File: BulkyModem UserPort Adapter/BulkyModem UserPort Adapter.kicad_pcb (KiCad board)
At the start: 2 copper layers, 70.7 x 35 mm, 7 parts, among them J1 C64_UserPort, J2 Temporary, J3 C64_Modem_IDC, M1 Mounting, M2 Mounting, M3 Mounting, M4 Mounting

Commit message: Add DCD
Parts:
- moved J3 10.5 mm to (156.6, 78.1), turned to 270 degrees
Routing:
- net Net-(J2-Pad4): track 7.40 -> 28.4 mm
- net Net-(J2-Pad6): track 7.40 -> 25.9 mm
- net Net-(J2-Pad8): track 7.40 -> 23.4 mm
- net Net-(J2-Pad10): track 7.40 -> 18.9 mm
- net RX: track 51.7 -> 43.7 mm
- net RTS: track 24.1 -> 26.7 mm, vias 0 -> 1
- net TX: track 48.8 -> 46.3 mm
- net DCD: track 20.3 -> 22.3 mm
- net Net-(J1-Pad6): track 25.7 -> 24.5 mm
- net CTS: track 20.8 -> 21.9 mm
- net Net-(J1-Pad2): track 42.9 -> 43.2 mm, vias 2 -> 1

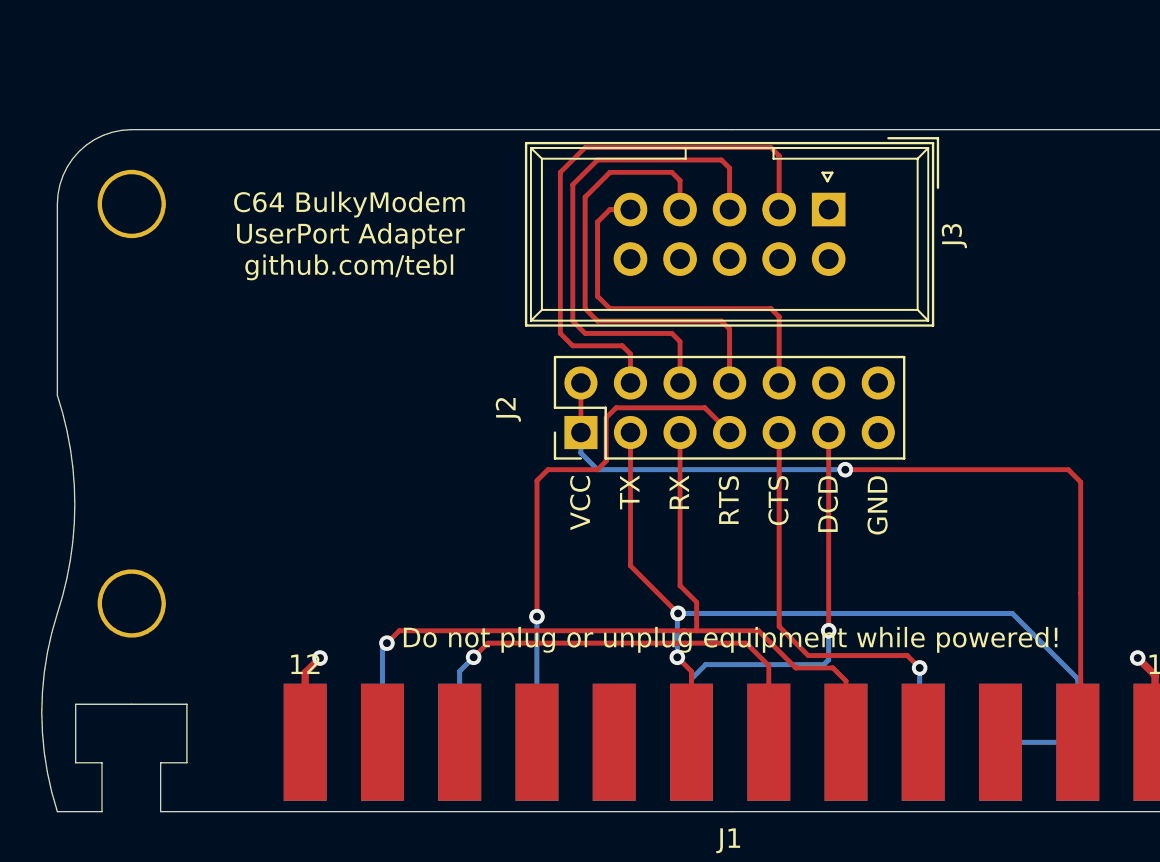
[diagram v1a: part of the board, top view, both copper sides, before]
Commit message: Changed IDC pin count
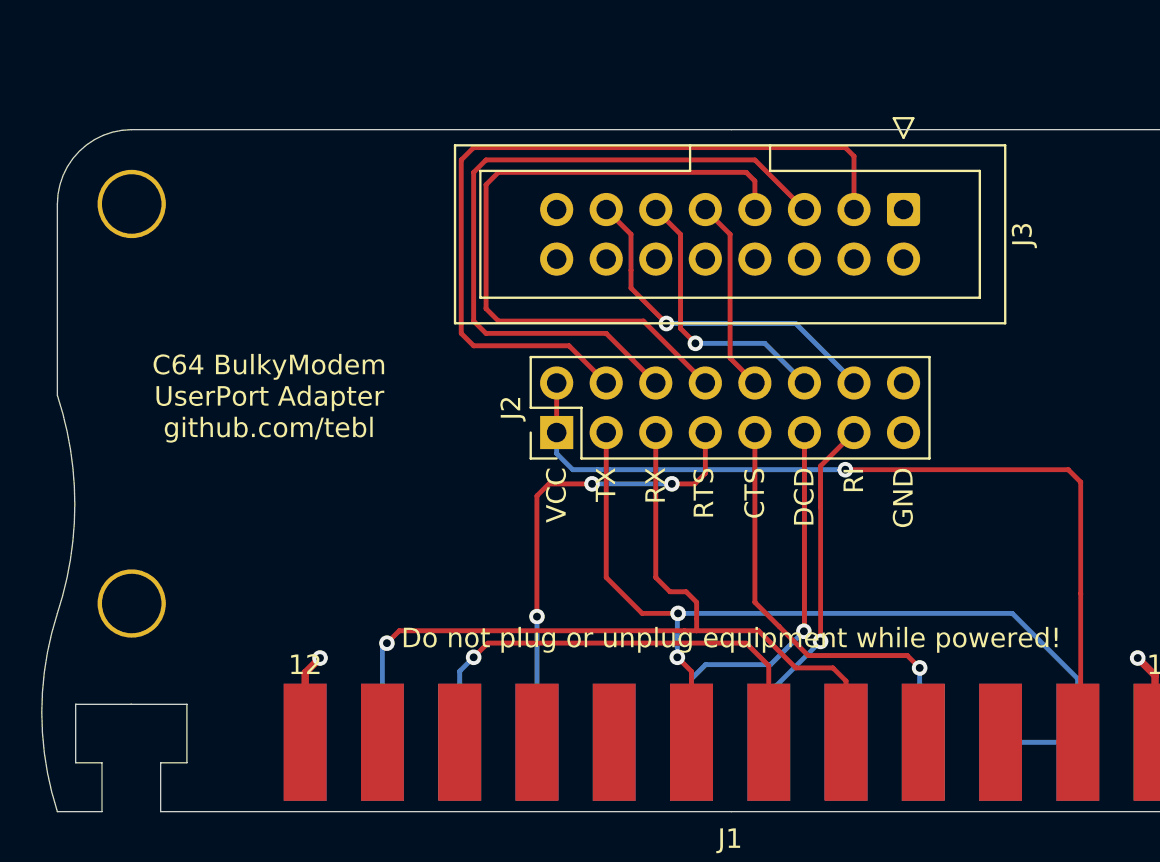
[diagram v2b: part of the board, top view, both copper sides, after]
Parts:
- J2: footprint Connector_PinHeader_2.54mm:PinHeader_2x07_P2.54mm_Vertical -> Connector_PinHeader_2.54mm:PinHeader_2x08_P2.54mm_Vertical
- J3: footprint BulkyModem:C64_Adapter_IDC -> BulkyModem:UserPort_Adapter_IDC
- moved J3 3.84 mm to (160.5, 78.1)
- moved J2 1.24 mm to (142.7, 89.5)
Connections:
- J1 pad 10: (no net) -> Net-(J1-Pad10)
- J1 pad 11: (no net) -> Net-(J1-Pad11)
- J1 pad 3: (no net) -> Net-(J1-Pad3)
- J1 pad 4: (no net) -> Net-(J1-Pad4)
- J1 pad 8: (no net) -> Net-(J1-Pad8)
- J1 pad 9: (no net) -> Net-(J1-Pad9)
- J1 pad E: (no net) -> Net-(J1-PadE)
- J1 pad F: (no net) -> RI
- J1 pad J: (no net) -> Net-(J1-PadJ)
- J2 pad 12: (no net) -> Net-(J2-Pad12)
- J2 pad 13: GND -> RI
- J2 pad 14: GND -> Net-(J2-Pad14)
- J3 pad 1: (no net) -> Net-(J3-Pad1)
- J3 pad 6: GND -> Net-(J2-Pad12)
- J3 pad 7: GND -> Net-(J2-Pad14)
- J3 pad 8: GND -> Net-(J3-Pad8)
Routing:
- net Net-(J2-Pad14): track 0.00 -> 18.0 mm, vias 0 -> 1
- net RI: track 0.00 -> 17.7 mm, vias 0 -> 1
- net Net-(J2-Pad12): track 0.00 -> 14.1 mm, vias 0 -> 1
- net Net-(J2-Pad4): track 28.4 -> 40.7 mm
- net Net-(J2-Pad8): track 23.4 -> 34.9 mm
- net Net-(J2-Pad6): track 25.9 -> 36.5 mm
- net Net-(J2-Pad10): track 18.9 -> 9.94 mm
- net RTS: track 26.7 -> 23.8 mm, vias 1 -> 3
- net DCD: track 22.3 -> 20.2 mm
- net TX: track 46.3 -> 47.9 mm
- net Net-(J1-Pad2): track 43.2 -> 44.5 mm
- net RX: track 43.7 -> 44.7 mm
- net CTS: track 21.9 -> 22.4 mm
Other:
- board text added: "RI"

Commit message: Alternate panel designs
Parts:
- removed J2: Temporary, Connector_PinHeader_2.54mm:PinHeader_2x08_P2.54mm_Vertical
- added G***: LOGO, artwork:BulkyModem_small, B.Cu at (151.6, 90.7)
- added JP1: UP9600, solder_bridge:bridge, F.Cu at (157.5, 97.5)
- added JP2: UP9600, solder_bridge:bridge, F.Cu at (149.6, 97.5)
- moved J3 5.00 mm to (160.5, 83.1)
- moved M3 5.00 mm to (182.4, 82.8)
- moved M4 5.00 mm to (120.9, 82.8)
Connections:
- J1 pad 10: Net-(J1-Pad10) -> (no net)
- J1 pad 11: Net-(J1-Pad11) -> (no net)
- J1 pad 2: Net-(J1-Pad2) -> (no net)
- J1 pad 3: Net-(J1-Pad3) -> (no net)
- J1 pad 4: Net-(J1-Pad4) -> (no net)
- J1 pad 5: RX -> Net-(J1-Pad5)
- J1 pad 7: TX -> Net-(J1-Pad7)
- J1 pad 8: Net-(J1-Pad8) -> (no net)
- J1 pad 9: Net-(J1-Pad9) -> (no net)
- J1 pad B: TX -> TXD
- J1 pad C: TX -> TXD
- J1 pad E: Net-(J1-PadE) -> (no net)
- J1 pad J: Net-(J1-PadJ) -> (no net)
- J1 pad M: RX -> RXD
- J3 pad 1: Net-(J3-Pad1) -> (no net)
- J3 pad 16: Net-(J3-Pad16) -> (no net)
- J3 pad 2: Net-(J2-Pad4) -> TXD
- J3 pad 3: Net-(J2-Pad6) -> RXD
- J3 pad 4: Net-(J2-Pad8) -> RTS
- J3 pad 5: Net-(J2-Pad10) -> CTS
- J3 pad 6: Net-(J2-Pad12) -> DCD
- J3 pad 7: Net-(J2-Pad14) -> RI
- J3 pad 8: Net-(J3-Pad8) -> (no net)
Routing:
- net RXD: track 0.00 -> 74.0 mm, vias 0 -> 2
- net TXD: track 0.00 -> 59.8 mm, vias 0 -> 1
- net TX: track 47.9 -> 0.00 mm, vias 2 -> 0
- net RX: track 44.7 -> 0.00 mm, vias 1 -> 0
- net Net-(J1-Pad2): track 44.5 -> 0.00 mm, vias 1 -> 0
- net Net-(J2-Pad4): track 40.7 -> 0.00 mm
- net Net-(J2-Pad6): track 36.5 -> 0.00 mm
- net Net-(J2-Pad8): track 34.9 -> 0.00 mm
- net Net-(J2-Pad14): track 18.0 -> 0.00 mm, vias 1 -> 0
- net Net-(J2-Pad12): track 14.1 -> 0.00 mm, vias 1 -> 0
- net RI: track 17.7 -> 30.9 mm
- net RTS: track 23.8 -> 36.9 mm, vias 3 -> 1
- net CTS: track 22.4 -> 34.2 mm
- net Net-(J2-Pad10): track 9.94 -> 0.00 mm
- net Net-(J1-Pad5): track 0.00 -> 7.89 mm
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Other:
- board size 70.7 x 35 mm -> 70.7 x 30 mm
- rule trace_min: 0.2 -> 0
- board text added: "Designed for use with"
- board text added: "Link for UP9600"
- board text removed: "CTS"
- board text removed: "DCD"
- board text removed: "Designed for use with BulkyModem."
- board text removed: "GND"
- board text removed: "RI"
- board text removed: "RTS"
- board text removed: "RX"
- board text removed: "TX"
- board text removed: "VCC"

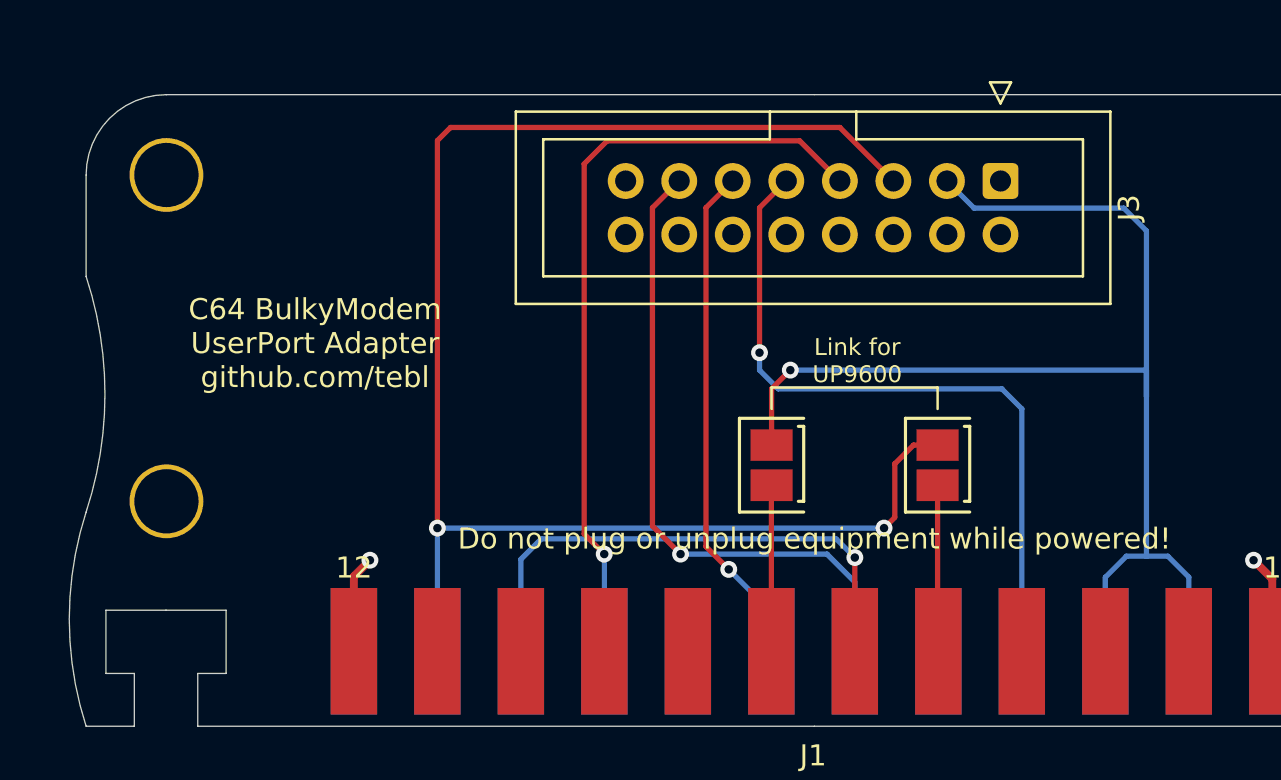
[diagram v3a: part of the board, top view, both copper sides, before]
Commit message: Updated UserPort layout
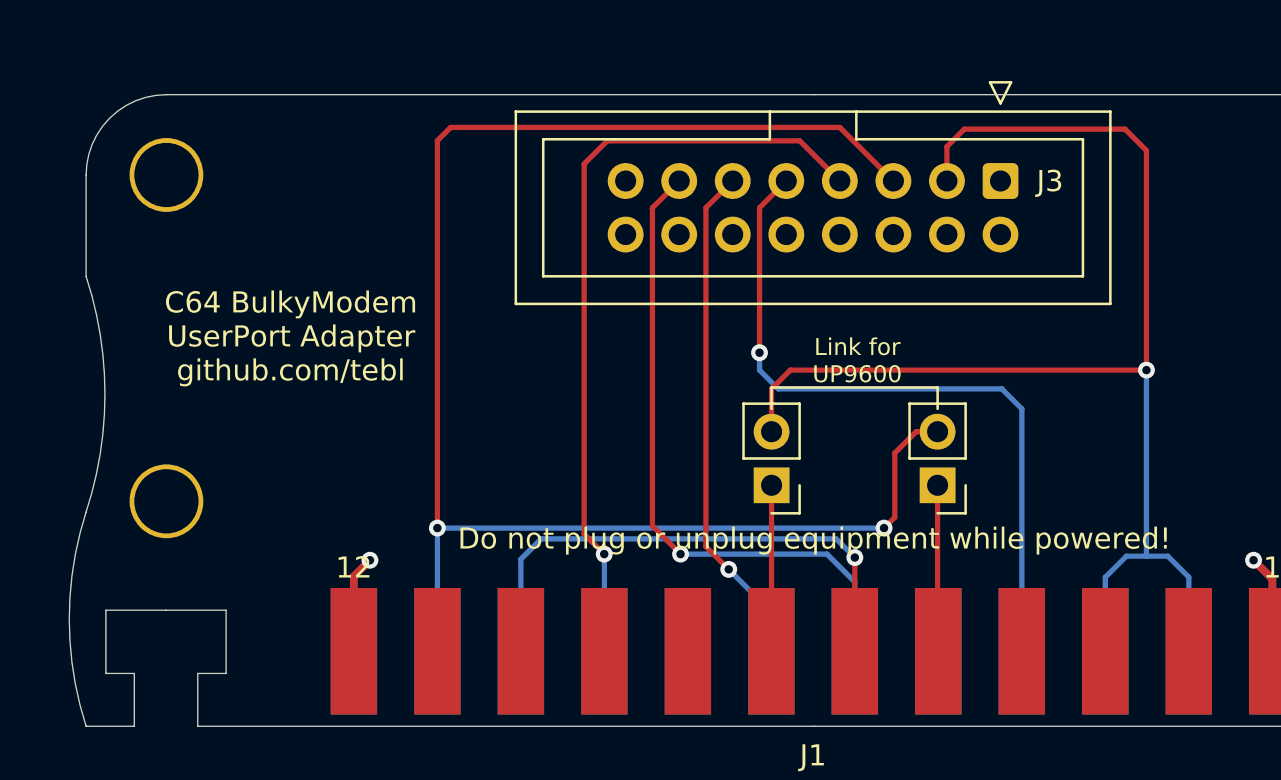
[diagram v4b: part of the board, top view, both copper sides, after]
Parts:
- JP1, JP2: footprint solder_bridge:bridge -> Connector_PinHeader_2.54mm:PinHeader_1x02_P2.54mm_Vertical
- moved G*** 0.32 mm to (151.6, 91.0)
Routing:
- net TXD: track 59.8 -> 63.1 mm
- net RXD: track 74.0 -> 74.6 mm

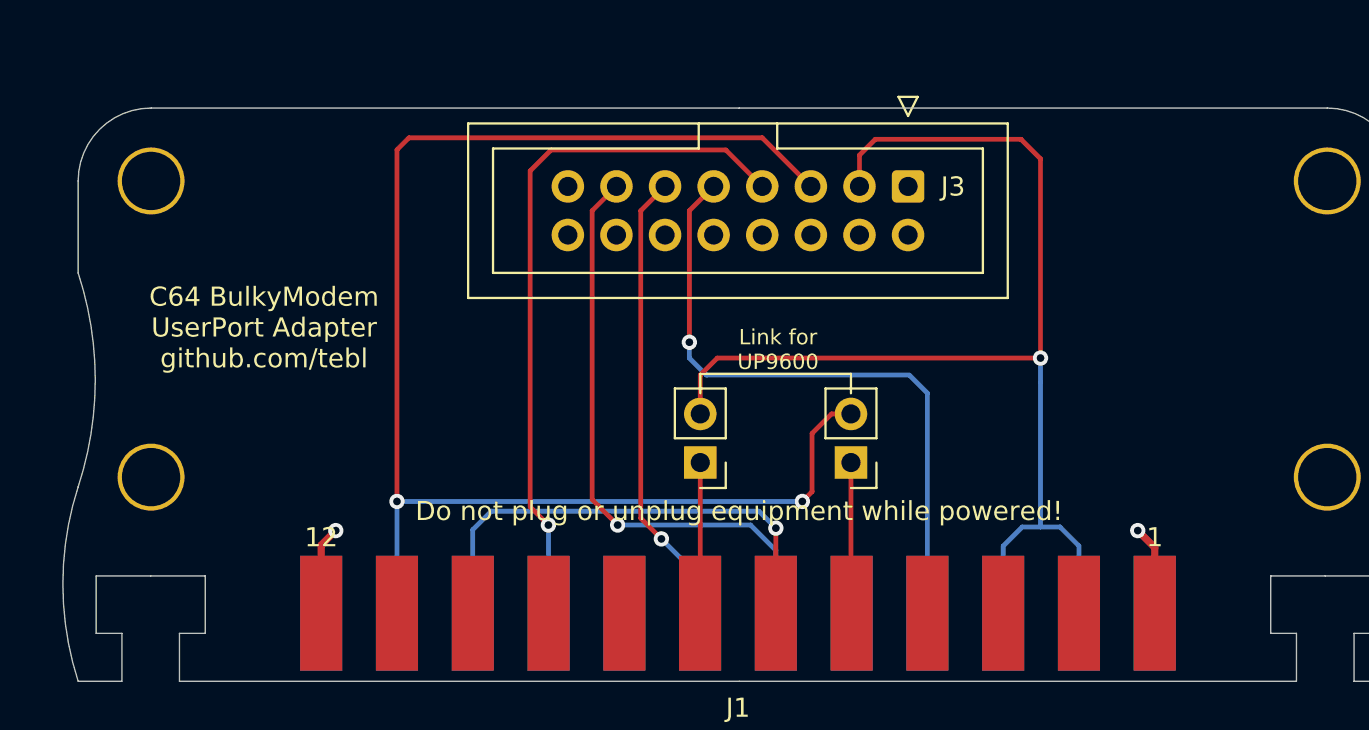
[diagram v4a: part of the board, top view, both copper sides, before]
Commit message: Moved UP9600 jumpers
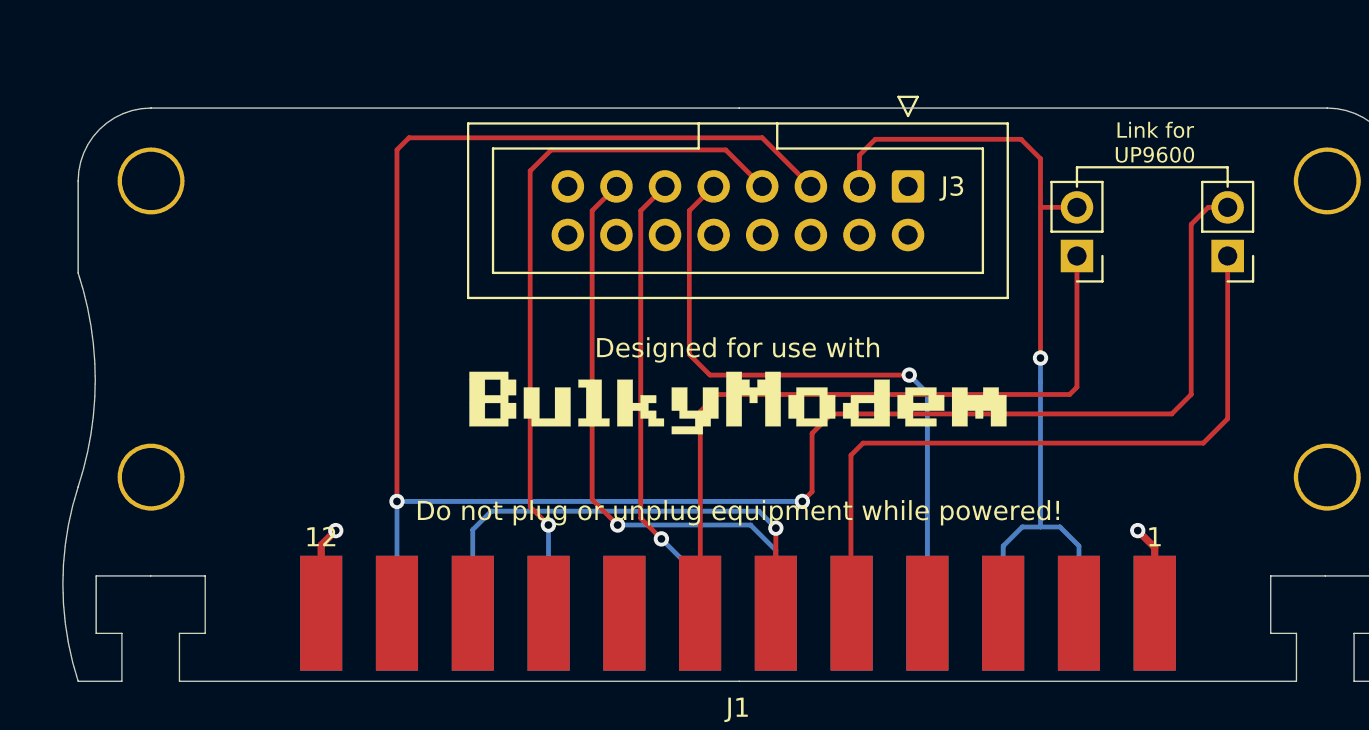
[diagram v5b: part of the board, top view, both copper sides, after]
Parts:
- G***: moved to F.Cu
- moved JP1 22.5 mm to (177.2, 86.7)
- moved JP2 22.5 mm to (169.3, 86.7)
- moved G*** 3.43 mm to (151.6, 94.4), turned to 0 degrees
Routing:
- net Net-(J1-Pad7): track 7.88 -> 37.6 mm
- net RXD: track 74.6 -> 103.9 mm
- net Net-(J1-Pad5): track 7.89 -> 37.3 mm
- net TXD: track 63.1 -> 44.8 mm
